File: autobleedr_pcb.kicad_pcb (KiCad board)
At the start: 4 copper layers, 43.4 x 104.3 mm, 23 parts, among them J11 Conn_01x02_Pin, J13 Screw_Terminal_01x08, J7 Screw_Terminal_01x02, Q1 PMOS, Q2 IRLML2060, SW1 SW_SPST, U2 ESP32, U6 TMC2209

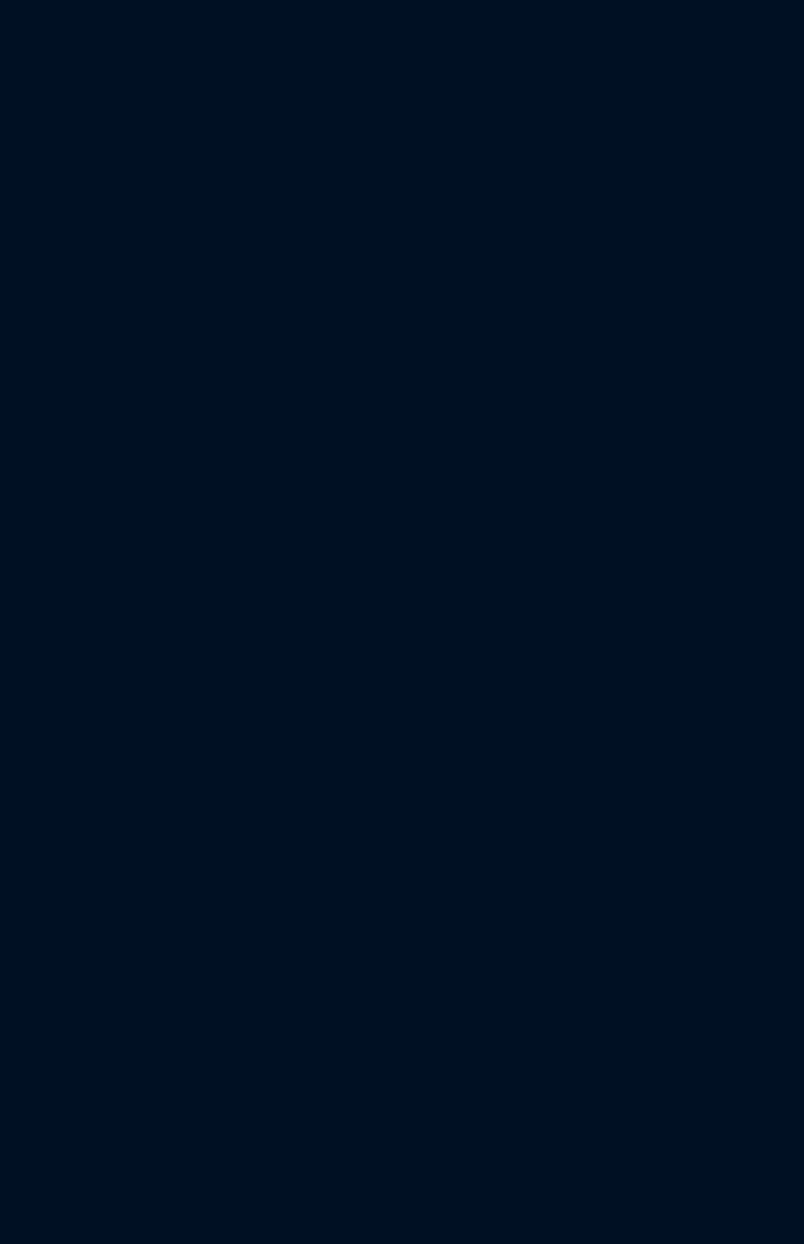
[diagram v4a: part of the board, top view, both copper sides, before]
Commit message: Added another rendition to the pcb layout
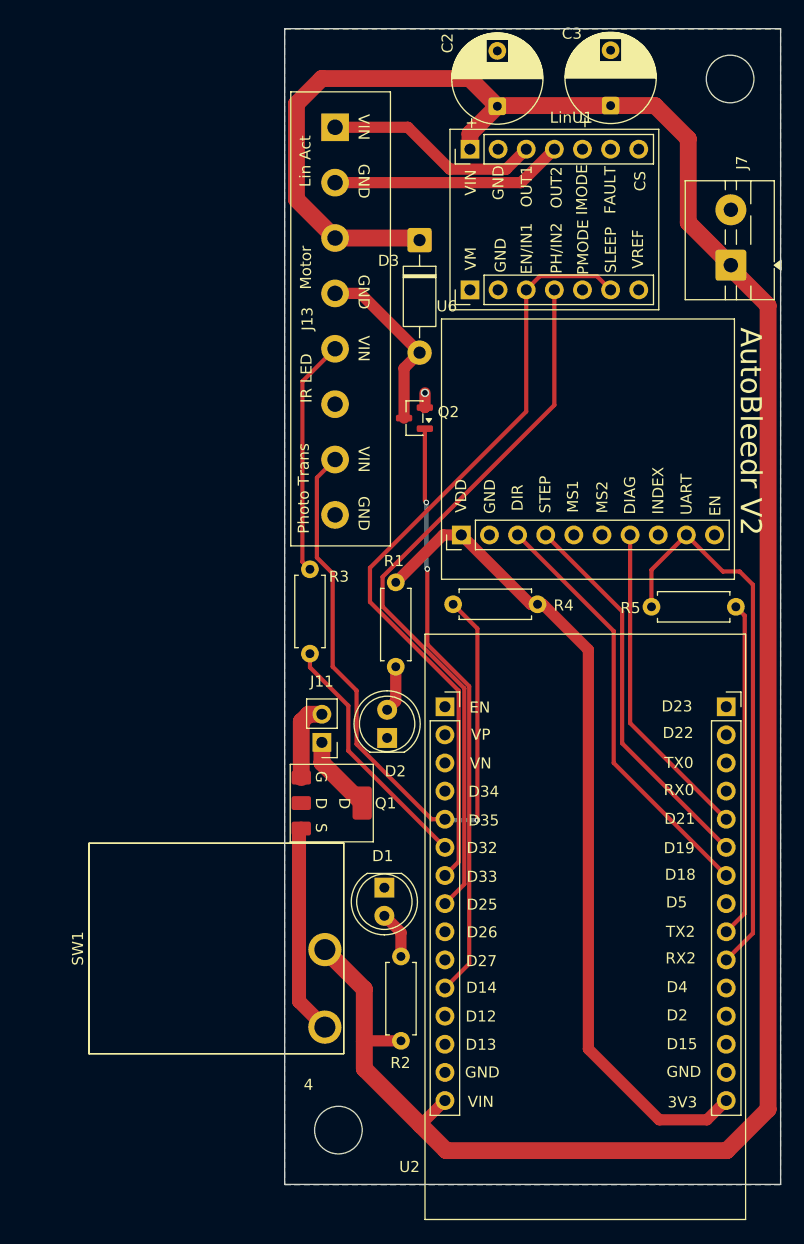
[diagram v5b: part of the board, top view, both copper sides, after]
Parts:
- added 2: MountingHole_4.3mm_M4_ISO7380_Pad, MountingHole:MountingHole_4.3mm_M4_ISO7380_Pad, F.Cu at (170.8, 76.3)
- added 4: MountingHole_4.3mm_M4_ISO7380_Pad, MountingHole:MountingHole_4.3mm_M4_ISO7380_Pad, F.Cu at (135.5, 171.2)
- added ?: , clipboard:eeda8126-6381-443f-87cd-efa4496c9bff, F.Cu at (190.7, 111.3)
- added C2: C_Polarized_US, Capacitor_THT:CP_Radial_D8.0mm_P5.00mm, F.Cu at (149.8, 78.7)
- added C3: C_Polarized_US, Capacitor_THT:CP_Radial_D8.0mm_P5.00mm, F.Cu at (160.0, 78.7)
- added D1: Power_LED, LED_THT:LED_D5.0mm_IRGrey, F.Cu at (139.6, 149.3)
- added D2: Power_LED, LED_THT:LED_D5.0mm_IRGrey, F.Cu at (139.9, 135.8)
- added D3: 1N4001, Diode_THT:D_DO-41_SOD81_P10.16mm_Horizontal, F.Cu at (142.8, 90.8)
- added J11: Conn_01x02_Pin, Connector_PinHeader_2.54mm:PinHeader_1x02_P2.54mm_Vertical, F.Cu at (134.0, 136.2)
- added J13: Screw_Terminal_01x08, Screw_Terminal_1x8:Screw_Terminal_1x8, F.Cu at (136.2, 97.9)
- added J7: Screw_Terminal_01x02, TerminalBlock:TerminalBlock_MaiXu_MX126-5.0-02P_1x02_P5.00mm, F.Cu at (170.9, 93.1)
- added LinU1: DVR8874, Capstone_Footprints:DVR8874, F.Cu at (145.5, 88.8)
- added Q1: PMOS, Capstone_Footprints:DMP6023LE, F.Cu at (135.1, 141.6)
- added Q2: IRLML2060, Package_TO_SOT_SMD:SOT-23, F.Cu at (142.3, 106.9)
- added R1: 220R, Resistor_THT:R_Axial_DIN0207_L6.3mm_D2.5mm_P7.62mm_Horizontal, F.Cu at (140.6, 129.3)
- added R2: 2k2R, Resistor_THT:R_Axial_DIN0207_L6.3mm_D2.5mm_P7.62mm_Horizontal, F.Cu at (141.1, 155.5)
- added R3: 220R, Resistor_THT:R_Axial_DIN0207_L6.3mm_D2.5mm_P7.62mm_Horizontal, F.Cu at (132.9, 128.1)
- added R4: 330kR, Resistor_THT:R_Axial_DIN0207_L6.3mm_D2.5mm_P7.62mm_Horizontal, F.Cu at (153.4, 123.7)
- added R5: 1500R, Resistor_THT:R_Axial_DIN0207_L6.3mm_D2.5mm_P7.62mm_Horizontal, F.Cu at (171.4, 123.9)
- added SW1: SW_SPST, Capstone_Footprints:R1966ABLKBLKGR, F.Cu at (123.9, 154.8)
- added U2: ESP32, Capstone_Footprints:ESP32, F.Cu at (145.2, 132.9)
- added U6: TMC2209, Capstone_Footprints:TMC2209, F.Cu at (157.9, 109.9)
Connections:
- U2 pad 10: /direction ERM DRV -> unconnected-(U2-D27-Pad10)
- U2 pad 9: /enable ERM DRV -> unconnected-(U2-D26-Pad9)
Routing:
- net +7.5V: track 147.9 -> 363.0 mm
- net +3.3V: track 135.4 -> 210.7 mm
- net /enable DRV: track 40.8 -> 112.0 mm
- net /linear actuator direction: track 36.4 -> 102.1 mm
- net D35: track 40.1 -> 102.1 mm, vias 2 -> 3
- net /speed ERM DRV: track 42.3 -> 95.4 mm, vias 0 -> 2
- net /TMC UART: track 72.7 -> 123.2 mm
- net /DIR: track 66.6 -> 105.2 mm
- net /STEP: track 61.8 -> 96.7 mm
- net Net-(U2-TX2): track 50.6 -> 81.0 mm
- net /DIAG: track 56.4 -> 85.6 mm
- net D32: track 22.7 -> 45.2 mm
- net /IR LED vin: track 22.6 -> 44.0 mm
- net /LIN ACT GND: track 45.1 -> 66.2 mm
- net /LIN ACT VIN: track 47.2 -> 66.8 mm
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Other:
- board size 43.4 x 104.3 mm -> 126.4 x 105.2 mm

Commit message: Redid pcb
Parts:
- removed the 2 at (170.8, 76.3)
- removed the 4 at (135.5, 171.2)
- removed the ? at (190.7, 111.3)
- removed C1: 0u1C, Capacitor_THT:C_Axial_L5.1mm_D3.1mm_P7.50mm_Horizontal
- removed the C2 at (149.8, 78.7)
- removed the C3 at (160.0, 78.7)
- removed the D1 at (139.6, 149.3)
- removed the D2 at (139.9, 135.8)
- removed the D3 at (142.8, 90.8)
- removed the J11 at (134.0, 136.2)
- removed the J13 at (136.2, 97.9)
- removed the J7 at (170.9, 93.1)
- removed the LinU1 at (145.5, 88.8)
- removed the Q1 at (135.1, 141.6)
- removed the Q2 at (142.3, 106.9)
- removed the R1 at (140.6, 129.3)
- removed the R2 at (141.1, 155.5)
- removed the R3 at (132.9, 128.1)
- removed the R4 at (153.4, 123.7)
- removed the R5 at (171.4, 123.9)
- removed the SW1 at (123.9, 154.8)
- removed the U2 at (145.2, 132.9)
- removed the U6 at (157.9, 109.9)
- moved C2 70.1 mm to (78.8, 80.1), turned to 90 degrees
- moved C3 60.9 mm to (68.8, 80.0)
- moved R1 30.5 mm to (58.4, 130.3), turned to 90 degrees
- moved LinU1 28.1 mm to (64.0, 90.4)
- moved D1 26.8 mm to (57.8, 149.9)
- moved R2 26.5 mm to (59.3, 156.1), turned to -90 degrees
- moved J7 23.5 mm to (88.9, 93.1), turned to 90 degrees
- moved R5 20.7 mm to (88.8, 124.8), turned to 180 degrees
- moved D3 20.5 mm to (61.0, 91.6)
- moved J11 20.2 mm to (52.5, 137.4)
- moved Q1 19.7 mm to (53.5, 143.6), turned to -90 degrees
- moved D2 17.3 mm to (58.0, 137.3), turned to 90 degrees
- moved U6 16.2 mm to (76.5, 111.1)
- moved SW1 16.1 mm to (42.5, 157.3)
- moved Q2 13.7 mm to (60.8, 106.7)
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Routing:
- net +7.5V: track 363.0 -> 214.5 mm
- net +3.3V: track 210.7 -> 75.0 mm, vias 2 -> 0
- net /TMC UART: track 123.2 -> 49.1 mm, vias 4 -> 0
- net /DIR: track 105.2 -> 37.6 mm
- net /STEP: track 96.7 -> 34.0 mm
- net /DIAG: track 85.6 -> 29.0 mm
- net Net-(U2-TX2): track 81.0 -> 30.4 mm
- net /LIN ACT VIN: track 66.8 -> 20.7 mm
- net /LIN ACT GND: track 66.2 -> 23.0 mm, vias 2 -> 0
- net D35: track 102.1 -> 59.3 mm, vias 3 -> 1
- net /speed ERM DRV: track 95.4 -> 53.6 mm
- net /enable DRV: track 112.0 -> 70.5 mm, vias 2 -> 0
- net /linear actuator direction: track 102.1 -> 65.0 mm, vias 2 -> 0
- net /ERM neg: track 43.8 -> 15.1 mm, vias 2 -> 0
- net D32: track 45.2 -> 21.0 mm, vias 2 -> 0
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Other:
- board size 126.4 x 105.2 mm -> 44.4 x 104.3 mm
- board text added: "D35"
- board text removed: "D33"

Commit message: Added EN pin and c1
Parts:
- added C1: 0u1C, Capacitor_THT:C_Axial_L5.1mm_D3.1mm_P7.50mm_Horizontal, F.Cu at (54.8, 122.7)
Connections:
- U2 pad 30: unconnected-(U2-D23-Pad30) -> /EN
- U6 pad 10: GND -> /EN
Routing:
- net /EN: track 0.00 -> 15.7 mm
- net /enable DRV: track 70.5 -> 79.3 mm
- net /linear actuator direction: track 65.0 -> 73.7 mm
- net +3.3V: track 75.0 -> 78.6 mm
- net D35: track 59.3 -> 60.7 mm

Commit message: Update bubble circuit
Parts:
- R1, R3: value 220R -> 180R
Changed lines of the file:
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@@
 			)
 		)
-		(property "Value" "220R"
+		(property "Value" "180R"
 			(at 3.81 2.37 90)
 			(layer "F.Fab")
@@
 			)
 		)
-		(property "Value" "220R"
+		(property "Value" "180R"
 			(at 3.81 2.37 90)
 			(layer "F.Fab")
